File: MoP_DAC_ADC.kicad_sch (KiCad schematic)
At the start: 7 parts, among them J17 ADC_{in}, U14 ADS1015IDGS, U15 ADS1015IDGS

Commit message: Finished schematics
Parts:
- C801: renamed from C4; footprint (none) -> Capacitor_SMD:C_0805_2012Metric_Pad1.18x1.45mm_HandSolder
- C802: renamed from C3; footprint (none) -> Capacitor_SMD:C_0805_2012Metric_Pad1.18x1.45mm_HandSolder
- J801: renamed from J17; footprint (none) -> Connector_PinHeader_1.00mm:PinHeader_2x04_P1.00mm_Vertical
- JP801: renamed from JP1; footprint (none) -> Connector_PinHeader_2.54mm:PinHeader_1x02_P2.54mm_Vertical
- R801: renamed from R1; footprint (none) -> Resistor_SMD:R_0805_2012Metric; now not fitted
- renumbered U14 to U801, U15 to U802
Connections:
- net ADC10 renamed PSYS
- net ADC11 renamed ICHG
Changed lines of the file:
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@@
-		)
-	)
-	(label "ADC11"
-		(at 201.93 73.66 180)
-		(fields_autoplaced yes)
-		(effects
-			(font
-				(size 1.27 1.27)
-			)
-			(justify right bottom)
 		)
 	)
@@
 			)
 			(justify left bottom)
-		)
-	)
-	(label "ADC10"
-		(at 201.93 71.12 180)
-		(fields_autoplaced yes)
-		(effects
-			(font
-				(size 1.27 1.27)
-			)
-			(justify right bottom)
 		)
 	)
@@
 		)
 	)
+	(hierarchical_label "ICHG"
+		(shape input)
+		(at 201.93 73.66 180)
+		(fields_autoplaced yes)
+		(effects
+			(font
+				(size 1.27 1.27)
+			)
+			(justify right)
+		)
+	)
+	(hierarchical_label "PSYS"
+		(shape input)
+		(at 201.93 71.12 180)
+		(fields_autoplaced yes)
+		(effects
+			(font
+				(size 1.27 1.27)
+			)
+			(justify right)
+		)
+	)
 	(symbol
 		(lib_id "power:GNDREF")
@@
 		(exclude_from_sim no)
 		(in_bom yes)
-		(on_board yes)
-		(dnp no)
-		(property "Reference" "R1"
+		(on_board no)
+		(dnp yes)
+		(property "Reference" "R801"
 			(at 50.8 43.434 90)
 			(effects
@@
 			)
 		)
-		(property "Footprint" ""
+		(property "Footprint" "Resistor_SMD:R_0805_2012Metric"
 			(at 50.8 42.418 90)
 			(effects
@@
 			(project "MoP"
 				(path "/4d76798e-9a11-4d8d-a723-72f274a89091/6a166328-b4f8-4957-9253-71d3eae4309f"
-					(reference "R1")
+					(reference "R801")
 					(unit 1)
 				)
@@
 		(on_board yes)
 		(dnp no)
-		(property "Reference" "U14"
+		(property "Reference" "U801"
 			(at 81.6259 46.99 0)
 			(effects
@@
 			(project ""
 				(path "/4d76798e-9a11-4d8d-a723-72f274a89091/6a166328-b4f8-4957-9253-71d3eae4309f"
-					(reference "U14")
+					(reference "U801")
 					(unit 1)
 				)
@@
 		(dnp no)
 		(fields_autoplaced yes)
-		(property "Reference" "C4"
+		(property "Reference" "C801"
 			(at 104.14 44.4499 0)
 			(effects
@@
 			)
 		)
-		(property "Footprint" ""
+		(property "Footprint" "Capacitor_SMD:C_0805_2012Metric_Pad1.18x1.45mm_HandSolder"
 			(at 101.2952 49.53 0)
 			(effects
@@
 			(project "MoP"
 				(path "/4d76798e-9a11-4d8d-a723-72f274a89091/6a166328-b4f8-4957-9253-71d3eae4309f"
-					(reference "C4")
+					(reference "C801")
 					(unit 1)
 				)
@@
 		(on_board yes)
 		(dnp no)
-		(property "Reference" "U15"
+		(property "Reference" "U802"
 			(at 81.6259 102.87 0)
 			(effects
@@
 			(project "MoP"
 				(path "/4d76798e-9a11-4d8d-a723-72f274a89091/6a166328-b4f8-4957-9253-71d3eae4309f"
-					(reference "U15")
+					(reference "U802")
 					(unit 1)
 				)
@@
 		(dnp no)
 		(fields_autoplaced yes)
-		(property "Reference" "J17"
+		(property "Reference" "J801"
 			(at 199.39 82.55 0)
 			(effects
@@
 			)
 		)
-		(property "Footprint" ""
+		(property "Footprint" "Connector_PinHeader_1.00mm:PinHeader_2x04_P1.00mm_Vertical"
 			(at 200.66 91.44 0)
 			(effects
@@
 			(project "MoP"
 				(path "/4d76798e-9a11-4d8d-a723-72f274a89091/6a166328-b4f8-4957-9253-71d3eae4309f"
-					(reference "J17")
+					(reference "J801")
 					(unit 1)
 				)
@@
 		(dnp no)
 		(fields_autoplaced yes)
-		(property "Reference" "C3"
+		(property "Reference" "C802"
 			(at 104.14 100.3299 0)
 			(effects
@@
 			)
 		)
-		(property "Footprint" ""
+		(property "Footprint" "Capacitor_SMD:C_0805_2012Metric_Pad1.18x1.45mm_HandSolder"
 			(at 101.2952 105.41 0)
 			(effects
@@
 			(project ""
 				(path "/4d76798e-9a11-4d8d-a723-72f274a89091/6a166328-b4f8-4957-9253-71d3eae4309f"
-					(reference "C3")
+					(reference "C802")
 					(unit 1)
 				)
@@
 		(on_board yes)
 		(dnp no)
-		(property "Reference" "JP1"
+		(property "Reference" "JP801"
 			(at 50.8 34.544 0)
 			(effects
@@
 			)
 		)
-		(property "Footprint" ""
+		(property "Footprint" "Connector_PinHeader_2.54mm:PinHeader_1x02_P2.54mm_Vertical"
 			(at 50.8 36.83 0)
 			(effects
@@
 			(project "MoP"
 				(path "/4d76798e-9a11-4d8d-a723-72f274a89091/6a166328-b4f8-4957-9253-71d3eae4309f"
-					(reference "JP1")
-					(unit 1)
-				)
+					(reference "JP801")
+					(unit 1)
+				)

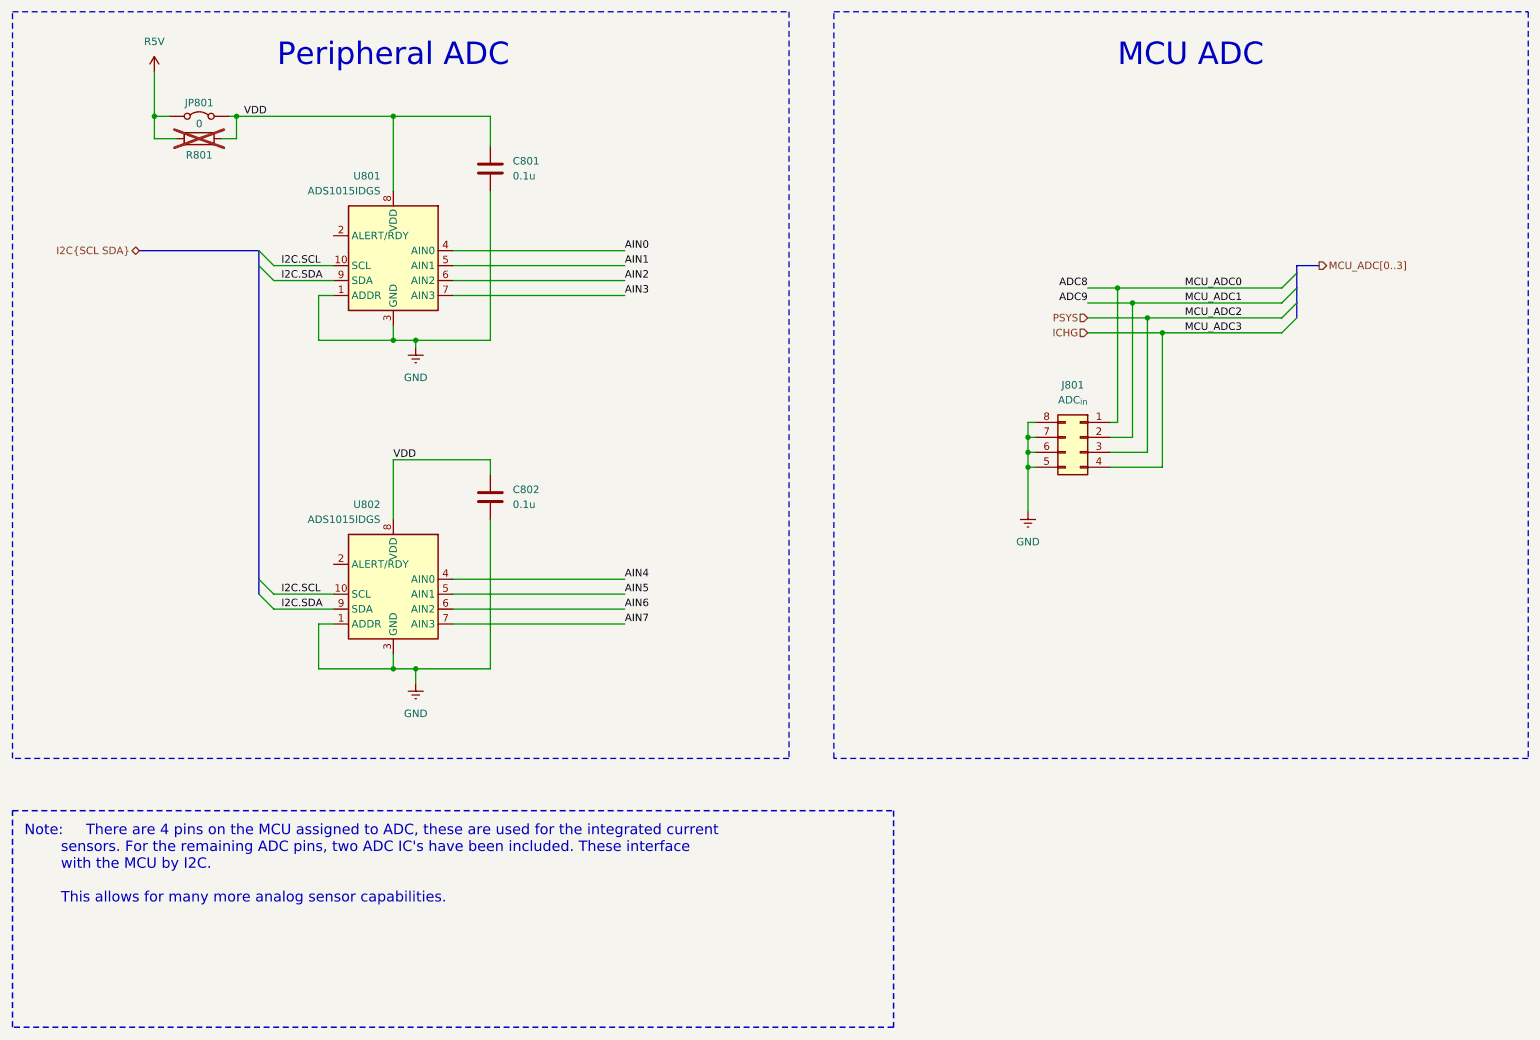
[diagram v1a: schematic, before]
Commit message: Added subproject for EPS PCB
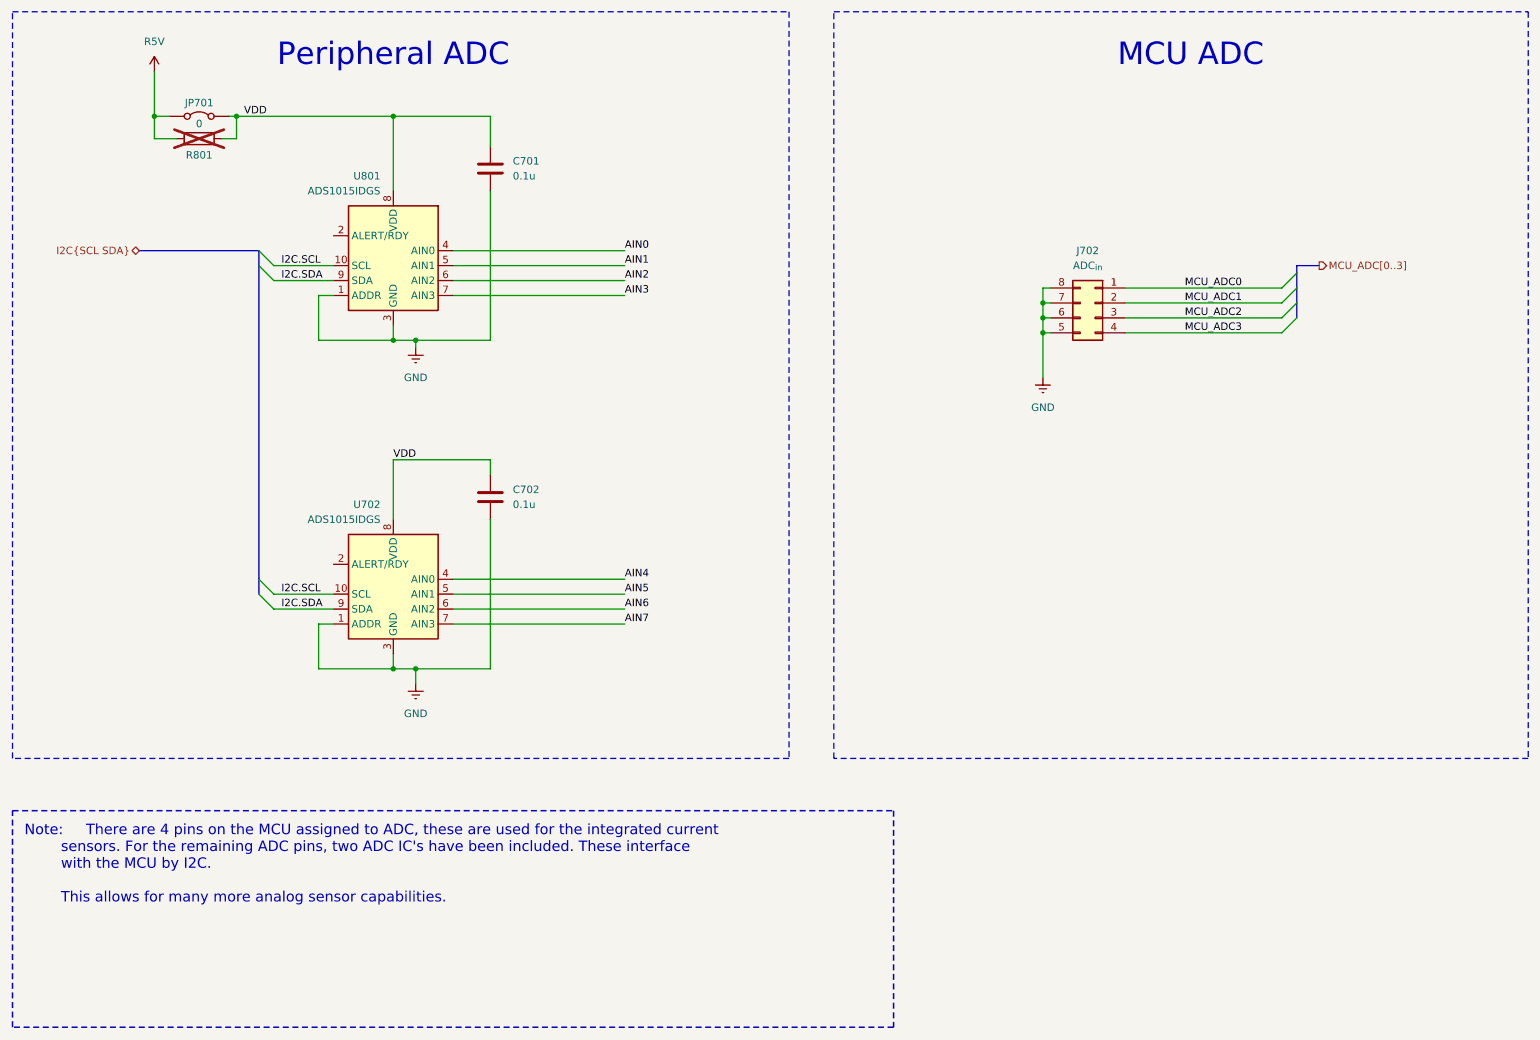
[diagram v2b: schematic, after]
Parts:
- J702: renamed from J801; footprint Connector_PinHeader_1.00mm:PinHeader_2x04_P1.00mm_Vertical -> Connector_PinHeader_2.54mm:PinHeader_1x04_P2.54mm_Vertical
- renumbered C801 to C701, C802 to C702, JP801 to JP701, U802 to U702
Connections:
- net ADC8 renamed MCU_ADC0
- net ADC9 renamed MCU_ADC1
- net ICHG renamed MCU_ADC3
- net PSYS renamed MCU_ADC2
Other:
- moved on the sheet: J702

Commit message: added OBC
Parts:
- removed J702: ADC_{in}, Connector_PinHeader_2.54mm:PinHeader_1x04_P2.54mm_Vertical, symbol Connector_Generic:Conn_02x04_Counter_Clockwise
- added J301: Conn_01x04, Connector_PinHeader_2.54mm:PinHeader_1x04_P2.54mm_Vertical, symbol Connector_Generic:Conn_01x03
- added J302, J303: Conn_01x04, Connector_PinHeader_2.54mm:PinHeader_1x04_P2.54mm_Vertical, symbol Connector_Generic:Conn_01x04
- added R302, R303: 10k, Resistor_SMD:R_0805_2012Metric, symbol Device:R
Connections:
- net AIN0: now also J302.1 (Pin_1)
- net AIN1: now also J302.2 (Pin_2)
- net AIN2: now also J302.3 (Pin_3)
- net AIN3: now also J302.4 (Pin_4)
- net AIN4: now also J303.1 (Pin_1)
- net AIN5: now also J303.2 (Pin_2)
- net AIN6: now also J303.3 (Pin_3)
- net AIN7: now also J303.4 (Pin_4)
- net MCU_ADC0: now also J301.3 (Pin_3)
- net MCU_ADC1: now also J301.2 (Pin_2)
- net MCU_ADC2: now also J301.1 (Pin_1)
- net VDD: now also R302.1, R303.1
- net at U801.2 (ALERT/RDY): now also R302.2
- net at U702.2 (ALERT/RDY): now also R303.2
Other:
- note added: "Note: There are 4 pins on the MCU assigned to ADC, these are used for the integrated current sensors. For the remaining ADC pins, two ADC IC's have been included. These interface with the MCU by I2C. This allows for many more analog sensor capabilities. The MCU ADC connector was not included on the final board since it takes up space and the headers on the MCU can be used, or the ADC chips."
- note removed: "Note: There are 4 pins on the MCU assigned to ADC, these are used for the integrated current sensors. For the remaining ADC pins, two ADC IC's have been included. These interface with the MCU by I2C. This allows for many more analog sensor capabilities."
